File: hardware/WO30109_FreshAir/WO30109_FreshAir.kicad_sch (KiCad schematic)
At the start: 44 parts, among them K1 G5Q-1 DC12, K2 G5Q-1 DC12, K3 G5Q-1 DC12, K4 G5Q-1 DC12, P1 AC IN, P2 SWD, P3 AC OUT, Q1 Si2302CDS, Q2 Si2302CDS, Q3 Si2302CDS, Q4 Si2302CDS, U1 STM32F103C8T6, U2 IRM-02-12, U3 ZS3L, U4 LM1117-3.3

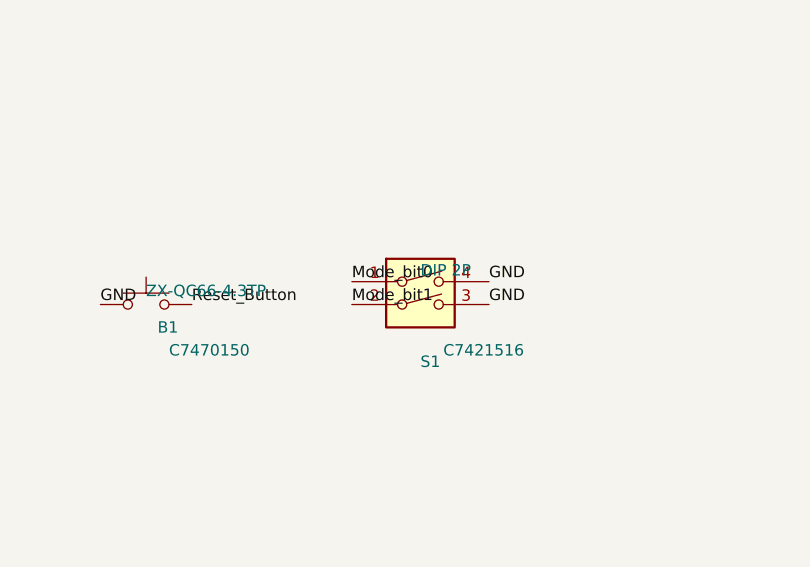
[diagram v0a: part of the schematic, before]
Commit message: feat: V1.3 PCB 由原 Gerber 轉入 KiCad＋安規 DRC 規則
- import_v13_pcb.py：走線/過孔照原樣、焊盤對齊放件、網路由銅箔連通推得
- 原理圖 vs 銅箔 0 衝突、parity 0；S1 Mode_bit 依銅箔修正
- .kicad_dru：市電↔SELV 6.4mm、市電間 2.5mm、板邊 0.5mm
- V1.3 DRC：253 個市電↔低壓違規（重現原設計問題）

Co-Authored-By: Claude Opus 5.5 (1M context) <noreply@anthropic.com>
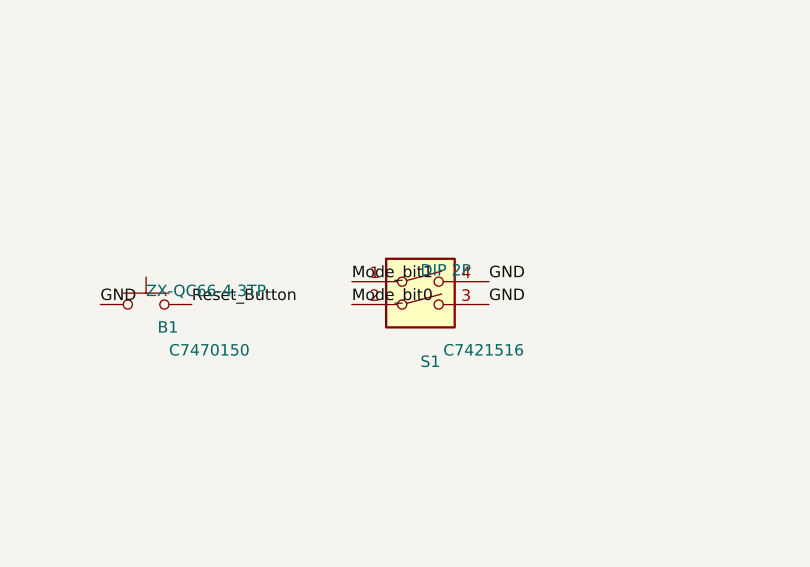
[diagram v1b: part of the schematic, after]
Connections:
- net Mode_bit0: now also S1.2; no longer S1.1
- net Mode_bit1: now also S1.1; no longer S1.2
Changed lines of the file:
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@@
 		(instances
 			(project "WO30109_FreshAir"
-				(path "/94552347-65ec-40ae-a746-f6e6e0667afa"
+				(path "/a2366431-4cde-4354-9495-6cae8083936f"
 					(reference "P1")
 					(unit 1)
@@
 		(instances
 			(project "WO30109_FreshAir"
-				(path "/94552347-65ec-40ae-a746-f6e6e0667afa"
+				(path "/a2366431-4cde-4354-9495-6cae8083936f"
 					(reference "U2")
 					(unit 1)
@@
 		(instances
 			(project "WO30109_FreshAir"
-				(path "/94552347-65ec-40ae-a746-f6e6e0667afa"
+				(path "/a2366431-4cde-4354-9495-6cae8083936f"
 					(reference "C6")
 					(unit 1)
@@
 		(instances
 			(project "WO30109_FreshAir"
-				(path "/94552347-65ec-40ae-a746-f6e6e0667afa"
+				(path "/a2366431-4cde-4354-9495-6cae8083936f"
 					(reference "U4")
 					(unit 1)
@@
 		(instances
 			(project "WO30109_FreshAir"
-				(path "/94552347-65ec-40ae-a746-f6e6e0667afa"
+				(path "/a2366431-4cde-4354-9495-6cae8083936f"
 					(reference "C7")
 					(unit 1)
@@
 		(instances
 			(project "WO30109_FreshAir"
-				(path "/94552347-65ec-40ae-a746-f6e6e0667afa"
+				(path "/a2366431-4cde-4354-9495-6cae8083936f"
 					(reference "U1")
 					(unit 1)
@@
 		(instances
 			(project "WO30109_FreshAir"
-				(path "/94552347-65ec-40ae-a746-f6e6e0667afa"
+				(path "/a2366431-4cde-4354-9495-6cae8083936f"
 					(reference "C1")
 					(unit 1)
@@
 		(instances
 			(project "WO30109_FreshAir"
-				(path "/94552347-65ec-40ae-a746-f6e6e0667afa"
+				(path "/a2366431-4cde-4354-9495-6cae8083936f"
 					(reference "C2")
 					(unit 1)
@@
 		(instances
 			(project "WO30109_FreshAir"
-				(path "/94552347-65ec-40ae-a746-f6e6e0667afa"
+				(path "/a2366431-4cde-4354-9495-6cae8083936f"
 					(reference "C3")
 					(unit 1)
@@
 		(instances
 			(project "WO30109_FreshAir"
-				(path "/94552347-65ec-40ae-a746-f6e6e0667afa"
+				(path "/a2366431-4cde-4354-9495-6cae8083936f"
 					(reference "C4")
 					(unit 1)
@@
 		(instances
 			(project "WO30109_FreshAir"
-				(path "/94552347-65ec-40ae-a746-f6e6e0667afa"
+				(path "/a2366431-4cde-4354-9495-6cae8083936f"
 					(reference "R1")
 					(unit 1)
@@
 		(instances
 			(project "WO30109_FreshAir"
-				(path "/94552347-65ec-40ae-a746-f6e6e0667afa"
+				(path "/a2366431-4cde-4354-9495-6cae8083936f"
 					(reference "C5")
 					(unit 1)
@@
 		(instances
 			(project "WO30109_FreshAir"
-				(path "/94552347-65ec-40ae-a746-f6e6e0667afa"
+				(path "/a2366431-4cde-4354-9495-6cae8083936f"
 					(reference "R2")
 					(unit 1)
@@
 		(instances
 			(project "WO30109_FreshAir"
-				(path "/94552347-65ec-40ae-a746-f6e6e0667afa"
+				(path "/a2366431-4cde-4354-9495-6cae8083936f"
 					(reference "R3")
 					(unit 1)
@@
 		(instances
 			(project "WO30109_FreshAir"
-				(path "/94552347-65ec-40ae-a746-f6e6e0667afa"
+				(path "/a2366431-4cde-4354-9495-6cae8083936f"
 					(reference "P2")
 					(unit 1)
@@
 		(instances
 			(project "WO30109_FreshAir"
-				(path "/94552347-65ec-40ae-a746-f6e6e0667afa"
+				(path "/a2366431-4cde-4354-9495-6cae8083936f"
 					(reference "U3")
 					(unit 1)
@@
 		(instances
 			(project "WO30109_FreshAir"
-				(path "/94552347-65ec-40ae-a746-f6e6e0667afa"
+				(path "/a2366431-4cde-4354-9495-6cae8083936f"
 					(reference "C8")
 					(unit 1)
@@
 		(instances
 			(project "WO30109_FreshAir"
-				(path "/94552347-65ec-40ae-a746-f6e6e0667afa"
+				(path "/a2366431-4cde-4354-9495-6cae8083936f"
 					(reference "C9")
 					(unit 1)
@@
 		(instances
 			(project "WO30109_FreshAir"
-				(path "/94552347-65ec-40ae-a746-f6e6e0667afa"
+				(path "/a2366431-4cde-4354-9495-6cae8083936f"
 					(reference "R4")
 					(unit 1)
@@
 		(instances
 			(project "WO30109_FreshAir"
-				(path "/94552347-65ec-40ae-a746-f6e6e0667afa"
+				(path "/a2366431-4cde-4354-9495-6cae8083936f"
 					(reference "L1")
 					(unit 1)
@@
 		(instances
 			(project "WO30109_FreshAir"
-				(path "/94552347-65ec-40ae-a746-f6e6e0667afa"
+				(path "/a2366431-4cde-4354-9495-6cae8083936f"
 					(reference "RF1")
 					(unit 1)
@@
 		(instances
 			(project "WO30109_FreshAir"
-				(path "/94552347-65ec-40ae-a746-f6e6e0667afa"
+				(path "/a2366431-4cde-4354-9495-6cae8083936f"
 					(reference "B1")
 					(unit 1)
@@
 		(instances
 			(project "WO30109_FreshAir"
-				(path "/94552347-65ec-40ae-a746-f6e6e0667afa"
+				(path "/a2366431-4cde-4354-9495-6cae8083936f"
 					(reference "S1")
 					(unit 1)
@@
 		(instances
 			(project "WO30109_FreshAir"
-				(path "/94552347-65ec-40ae-a746-f6e6e0667afa"
+				(path "/a2366431-4cde-4354-9495-6cae8083936f"
 					(reference "R5")
 					(unit 1)
@@
 		(instances
 			(project "WO30109_FreshAir"
-				(path "/94552347-65ec-40ae-a746-f6e6e0667afa"
+				(path "/a2366431-4cde-4354-9495-6cae8083936f"
 					(reference "R9")
 					(unit 1)
@@
 		(instances
 			(project "WO30109_FreshAir"
-				(path "/94552347-65ec-40ae-a746-f6e6e0667afa"
+				(path "/a2366431-4cde-4354-9495-6cae8083936f"
 					(reference "Q1")
 					(unit 1)
@@
 		(instances
 			(project "WO30109_FreshAir"
-				(path "/94552347-65ec-40ae-a746-f6e6e0667afa"
+				(path "/a2366431-4cde-4354-9495-6cae8083936f"
 					(reference "D1")
 					(unit 1)
@@
 		(instances
 			(project "WO30109_FreshAir"
-				(path "/94552347-65ec-40ae-a746-f6e6e0667afa"
+				(path "/a2366431-4cde-4354-9495-6cae8083936f"
 					(reference "K1")
 					(unit 1)
@@
 		(instances
 			(project "WO30109_FreshAir"
-				(path "/94552347-65ec-40ae-a746-f6e6e0667afa"
+				(path "/a2366431-4cde-4354-9495-6cae8083936f"
 					(reference "R6")
 					(unit 1)
@@
 		(instances
 			(project "WO30109_FreshAir"
-				(path "/94552347-65ec-40ae-a746-f6e6e0667afa"
+				(path "/a2366431-4cde-4354-9495-6cae8083936f"
 					(reference "R10")
 					(unit 1)
@@
 		(instances
 			(project "WO30109_FreshAir"
-				(path "/94552347-65ec-40ae-a746-f6e6e0667afa"
+				(path "/a2366431-4cde-4354-9495-6cae8083936f"
 					(reference "Q2")
 					(unit 1)
@@
 		(instances
 			(project "WO30109_FreshAir"
-				(path "/94552347-65ec-40ae-a746-f6e6e0667afa"
+				(path "/a2366431-4cde-4354-9495-6cae8083936f"
 					(reference "D2")
 					(unit 1)
@@
 		(instances
 			(project "WO30109_FreshAir"
-				(path "/94552347-65ec-40ae-a746-f6e6e0667afa"
+				(path "/a2366431-4cde-4354-9495-6cae8083936f"
 					(reference "K2")
 					(unit 1)
@@
 		(instances
 			(project "WO30109_FreshAir"
-				(path "/94552347-65ec-40ae-a746-f6e6e0667afa"
+				(path "/a2366431-4cde-4354-9495-6cae8083936f"
 					(reference "R7")
 					(unit 1)
@@
 		(instances
 			(project "WO30109_FreshAir"
-				(path "/94552347-65ec-40ae-a746-f6e6e0667afa"
+				(path "/a2366431-4cde-4354-9495-6cae8083936f"
 					(reference "R11")
 					(unit 1)
@@
 		(instances
 			(project "WO30109_FreshAir"
-				(path "/94552347-65ec-40ae-a746-f6e6e0667afa"
+				(path "/a2366431-4cde-4354-9495-6cae8083936f"
 					(reference "Q3")
 					(unit 1)
@@
 		(instances
 			(project "WO30109_FreshAir"
-				(path "/94552347-65ec-40ae-a746-f6e6e0667afa"
+				(path "/a2366431-4cde-4354-9495-6cae8083936f"
 					(reference "D3")
 					(unit 1)
@@
 		(instances
 			(project "WO30109_FreshAir"
-				(path "/94552347-65ec-40ae-a746-f6e6e0667afa"
+				(path "/a2366431-4cde-4354-9495-6cae8083936f"
 					(reference "K3")
 					(unit 1)
@@
 		(instances
 			(project "WO30109_FreshAir"
-				(path "/94552347-65ec-40ae-a746-f6e6e0667afa"
+				(path "/a2366431-4cde-4354-9495-6cae8083936f"
 					(reference "R8")
 					(unit 1)
@@
 		(instances
 			(project "WO30109_FreshAir"
-				(path "/94552347-65ec-40ae-a746-f6e6e0667afa"
+				(path "/a2366431-4cde-4354-9495-6cae8083936f"
 					(reference "R12")
 					(unit 1)
@@
 		(instances
 			(project "WO30109_FreshAir"
-				(path "/94552347-65ec-40ae-a746-f6e6e0667afa"
+				(path "/a2366431-4cde-4354-9495-6cae8083936f"
 					(reference "Q4")
 					(unit 1)
@@
 		(instances
 			(project "WO30109_FreshAir"
-				(path "/94552347-65ec-40ae-a746-f6e6e0667afa"
+				(path "/a2366431-4cde-4354-9495-6cae8083936f"
 					(reference "D4")
 					(unit 1)
@@
 		(instances
 			(project "WO30109_FreshAir"
-				(path "/94552347-65ec-40ae-a746-f6e6e0667afa"
+				(path "/a2366431-4cde-4354-9495-6cae8083936f"
 					(reference "K4")
 					(unit 1)
@@
 		(instances
 			(project "WO30109_FreshAir"
-				(path "/94552347-65ec-40ae-a746-f6e6e0667afa"
+				(path "/a2366431-4cde-4354-9495-6cae8083936f"
 					(reference "P3")
 					(unit 1)
@@
 		(instances
 			(project "WO30109_FreshAir"
-				(path "/94552347-65ec-40ae-a746-f6e6e0667afa"
+				(path "/a2366431-4cde-4354-9495-6cae8083936f"
 					(reference "#FLG01")
 					(unit 1)
@@
 		(instances
 			(project "WO30109_FreshAir"
-				(path "/94552347-65ec-40ae-a746-f6e6e0667afa"
+				(path "/a2366431-4cde-4354-9495-6cae8083936f"
 					(reference "#FLG02")
 					(unit 1)
@@
 		)
 	)
-	(label "Mode_bit0"
+	(label "Mode_bit1"
 		(at 322.58 101.6 0)
 		(effects
@@
 		)
 	)
-	(label "Mode_bit1"
+	(label "Mode_bit0"
 		(at 322.58 104.14 0)
 		(effects

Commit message: feat(v2.0): 原理圖改版 — 保險絲/壓敏電阻、降壓電源、ZS3L UART
- F1 T3.15A 慢斷保險絲（AC_L 入口）、RV1 07D471K 壓敏電阻
- U4 LM1117 -> AP63203WU 3.3V 降壓（L2 3.9uH、C7/C13 22uF、C12 BST 100nF，依規格書 Table 2）
- 12V 預算 146mA < IRM-02-12 167mA，保留原電源
- ZS3L TXD->PA10、RXD<-PA9（USART1）、RST<-PB1(+R13 10k)；LED 改 PB0
- NRST 電容 1uF->100nF、VDDA 加 C10 1uF、BOOT0 測試點 TP1
- ERC 0 error

Co-Authored-By: Claude Opus 5.5 (1M context) <noreply@anthropic.com>
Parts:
- removed U4: LM1117-3.3, Package_TO_SOT_SMD:SOT-223-3_TabPin2, symbol Regulator_Linear:AMS1117-3.3
- added C10: 1uF, Capacitor_SMD:C_0603_1608Metric, symbol Device:C
- added C12, C14: 100nF, Capacitor_SMD:C_0603_1608Metric, symbol Device:C
- added C13: 22uF 25V, Capacitor_SMD:C_0805_2012Metric, symbol Device:C
- added F1: T3.15A 250V, Fuse:Fuseholder_TR5_Littelfuse_No560_No460, symbol Device:Fuse
- added L2: 3.9uH, Inductor_SMD:L_Sunlord_SWPA4030S, symbol Device:L
- added R13: 10k, Resistor_SMD:R_0603_1608Metric, symbol Device:R
- added RV1: 07D471K, Varistor:RV_Disc_D7mm_W3.4mm_P5mm, symbol Device:Varistor
- added TP1: BOOT0, TestPoint:TestPoint_Pad_D1.5mm, symbol Connector:TestPoint
- added U4: AP63203WU-7, Package_TO_SOT_SMD:TSOT-23-6, symbol Regulator_Switching:AP63203WU
- C5: value 1uF -> 100nF; LCSC C15849 -> C14663
- C7: value 10uF -> 22uF 25V; footprint Capacitor_SMD:C_0603_1608Metric -> Capacitor_SMD:C_0805_2012Metric; LCSC C96446 -> C45783
- P1: value AC IN -> AC IN 230V
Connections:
- net +12V: now also C14.1, U4.2 (EN), U4.3 (IN)
- net +3V3: now also C10.1, C13.1, L2.2, R13.1, U4.1 (FB)
- net AC_L: now also F1.2, RV1.1; no longer P1.1 (Pin_1)
- net AC_N: now also RV1.2
- net BOOT0: now also TP1.1
- net GND: now also C10.2, C13.2, C14.2, U4.4 (GND)
- net LED: now reaches U1.18 (PB0)
- net LED: now also R4.1
- net ZB_RST: now reaches U1.19 (PB1)
- net ZB_RST: now also U3.1 (RST), R13.2
- net ZB_RX: now reaches U1.30 (PA9)
- net ZB_RX: now also U3.15 (RXD)
- net ZB_TX: now reaches U1.31 (PA10)
- net ZB_TX: now also U3.16 (TXD)
- removed net NET_LED: R4.1, U3.16 (TXD)
- new net AC_L_IN: F1.1, P1.1 (Pin_1)
- new net BST: C12.1, U4.6 (BST)
- new net SW: C12.2, L2.1, U4.5 (SW)
- no-connect marks 22 -> 16

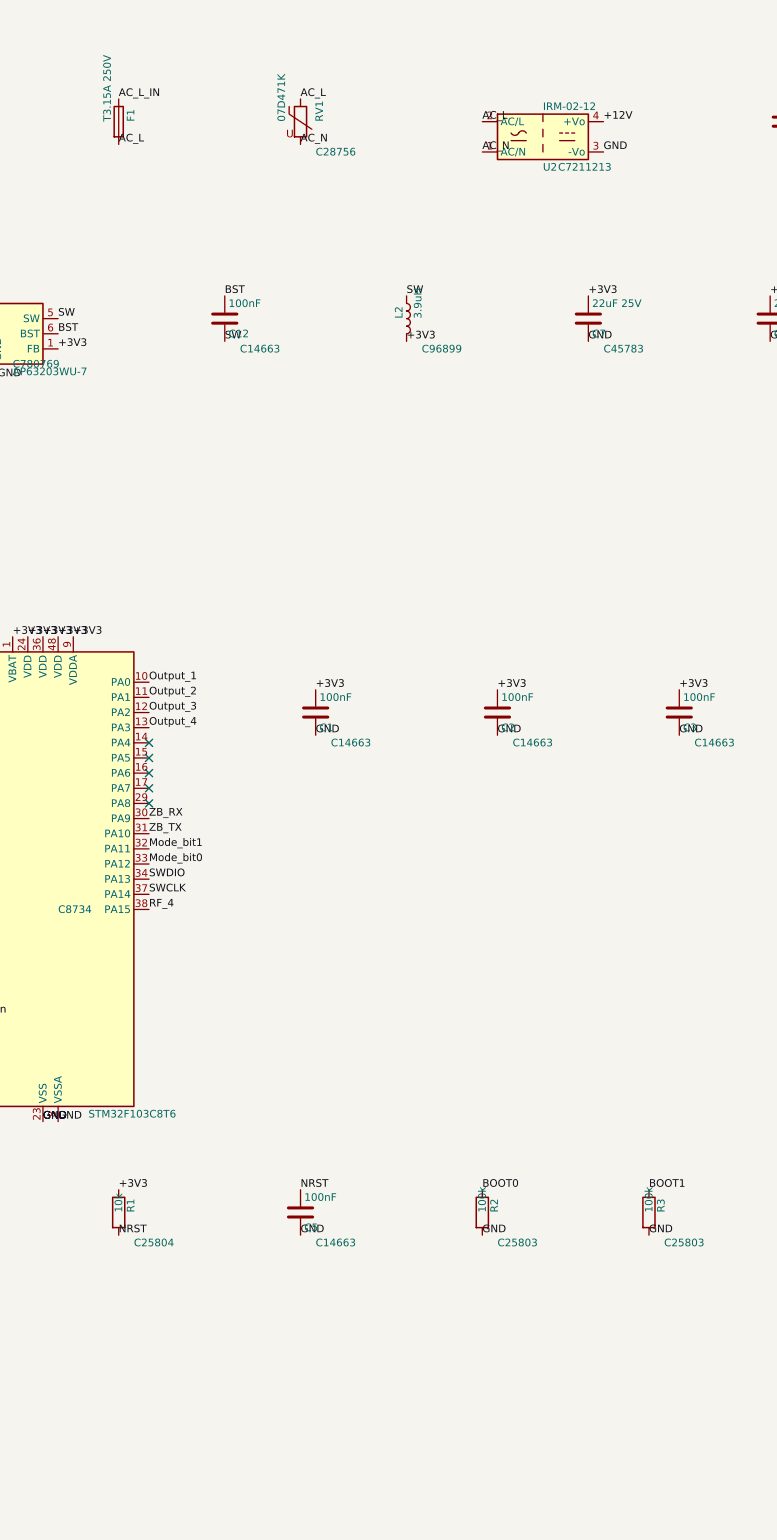
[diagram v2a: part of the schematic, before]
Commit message: feat(v2.0): PCB 安規改版完成 — DRC 0 錯誤、全部接通
PCB
- 市電↔低壓 ≥6.4mm、市電網路間 ≥1.5mm、板邊 ≥0.5mm（.kicad_dru 規則）
- 新增固定孔到市電 ≥2.3mm 規則；右緣市電走道外移、AC_N 在 H2 旁內彎（H2 0.85→2.85mm）
- F1/RV1、AP63203 降壓、繼電器驅動、RF1/P2/S1 重新擺放；H1–H4 固定孔
- 繼電器輸出 DO_* 由 mains_router 雙層格點佈線；低壓由 Freerouting，剩餘由 route_leftovers 補
- GND 鋪銅依規則自動退讓；LCSC 料號不印絲印

工具與文件
- scripts/build_v20.sh 一鍵重建（多組 Freerouting 設定，取第一組全接通）
- .github/workflows/kicad-ci.yml：ERC/DRC/生產檔
- README：架構、改版、安規、版控、CI、範例（mermaid 圖）＋板子圖片
- docs/review：V1.3 設計審查

驗證（kicad-cli 10.0.6）：ERC 0、DRC 0 錯誤、0 未連線、0 parity

Co-Authored-By: Claude Opus 5.5 (1M context) <noreply@anthropic.com>
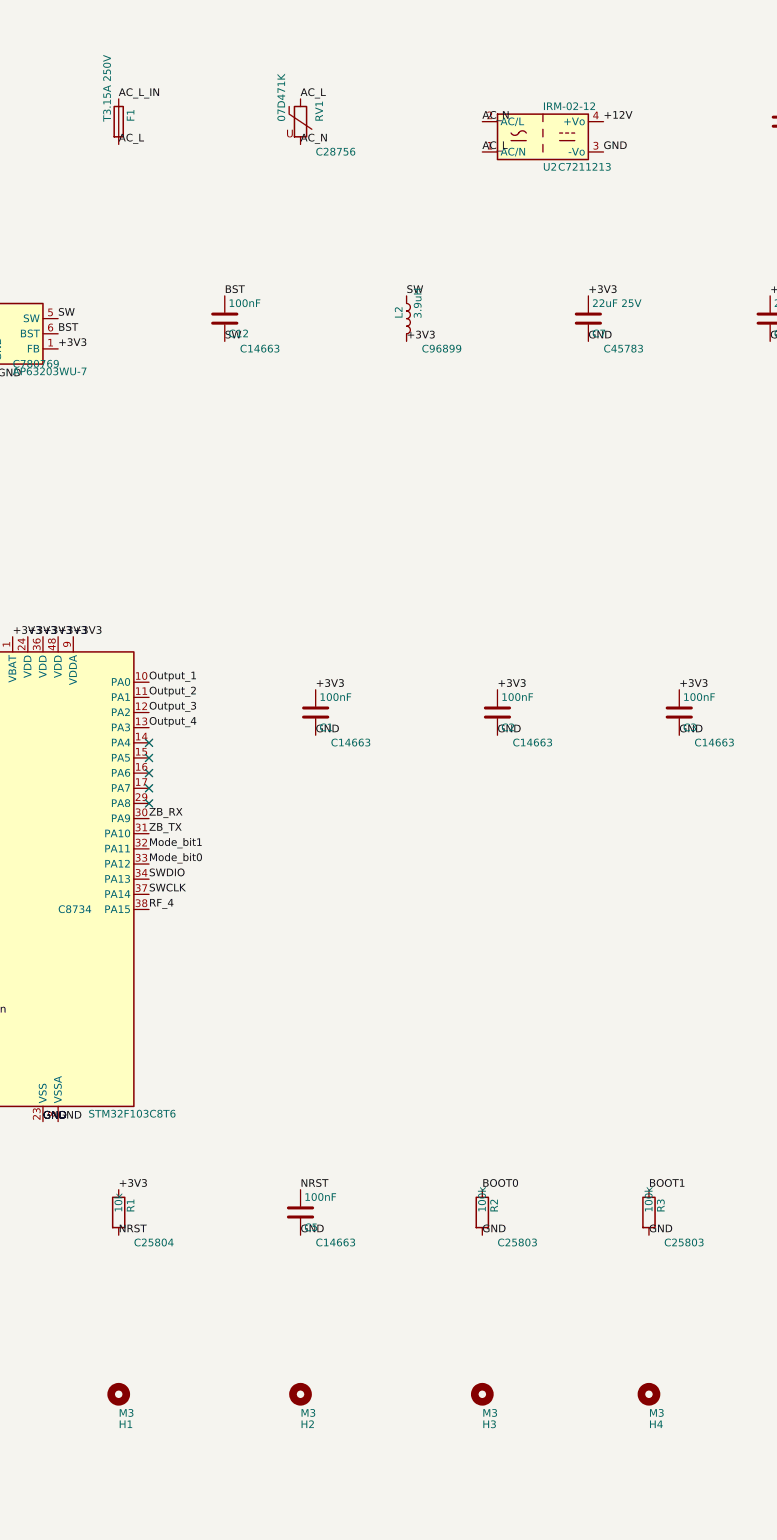
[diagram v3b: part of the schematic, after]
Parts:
- added H1, H2, H3, H4: M3, MountingHole:MountingHole_3.2mm_M3, symbol Mechanical:MountingHole
- K1, K2, K3, K4: footprint Relay_THT:Relay_SPDT_Omron-G5Q-1 -> WOOW:Relay_SPDT_Omron-G5Q-1_Tight
- TP1: now left out of the parts list
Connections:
- net AC_L: now also U2.1 (AC/N); no longer U2.2 (AC/L)
- net AC_N: now also U2.2 (AC/L); no longer U2.1 (AC/N)

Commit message: feat(v3.0): Tuya ZS3L＋EPA09-4D → ESP32-C6 單晶片＋SYN480R
- U1 STM32F103＋U3 ZS3L → ESP32-C6-WROOM-1-N8（C5366877，Zigbee 3.0，JLC 有庫存）
- RF1 EPA09-4D → SYN480R（C916347）＋13.52127MHz 晶振＋LC 匹配，韌體解 EV1527
- B1 改 IO9（BOOT），P2 改 2×3 燒錄座；ANT1 433MHz 天線焊點
- PCB 從 v2.0 標籤開始，只動低壓區；build_v30.sh 一鍵重建
- 檢查：ERC 0 錯誤、DRC 0 錯誤、0 未連線、parity 0

Co-Authored-By: Claude Opus 5.5 (1M context) <noreply@anthropic.com>
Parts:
- removed C10: 1uF, Capacitor_SMD:C_0603_1608Metric, symbol Device:C
- removed C3, C4: 100nF, Capacitor_SMD:C_0603_1608Metric, symbol Device:C
- removed P2: SWD, Connector_PinHeader_2.54mm:PinHeader_1x04_P2.54mm_Vertical, symbol Connector_Generic:Conn_01x04
- removed R13: 10k, Resistor_SMD:R_0603_1608Metric, symbol Device:R
- removed RF1: EPA09-4D, WOOW:Ebelong_EPA09-4D, symbol WOOW:EPA09-4D
- removed TP1: BOOT0, TestPoint:TestPoint_Pad_D1.5mm, symbol Connector:TestPoint
- removed U1: STM32F103C8T6, Package_QFP:LQFP-48_7x7mm_P0.5mm, symbol MCU_ST_STM32F1:STM32F103C8Tx
- removed U3: ZS3L, WOOW:Tuya_ZS3L, symbol WOOW:ZS3L
- added ANT1: 433MHz 1/4λ 17.3cm, TestPoint:TestPoint_THTPad_D2.0mm_Drill1.0mm, symbol Connector:Conn_01x01_Pin
- added C15: 6.8pF C0G, Capacitor_SMD:C_0603_1608Metric, symbol Device:C
- added C16: 1.8pF C0G, Capacitor_SMD:C_0603_1608Metric, symbol Device:C
- added C17: 1uF, Capacitor_SMD:C_0603_1608Metric, symbol Device:C
- added L3: 27nH, Inductor_SMD:L_0603_1608Metric, symbol Device:L
- added L4: 47nH, Inductor_SMD:L_0603_1608Metric, symbol Device:L
- added P2: PROG, Connector_PinHeader_2.54mm:PinHeader_2x03_P2.54mm_Vertical, symbol Connector_Generic:Conn_02x03_Odd_Even
- added R14: 0R, Resistor_SMD:R_0603_1608Metric, symbol Device:R
- added U1: ESP32-C6-WROOM-1-N8, WOOW:Espressif_ESP32-C6-WROOM-1, symbol WOOW:ESP32-C6-WROOM-1
- added U3: SYN480R, Package_SO:SOIC-8_3.9x4.9mm_P1.27mm, symbol WOOW:SYN480R
- added Y1: 13.52127MHz 20pF, Crystal:Crystal_SMD_3225-4Pin_3.2x2.5mm, symbol WOOW:Crystal_4P
- C1: value 100nF -> 22uF 25V; footprint Capacitor_SMD:C_0603_1608Metric -> Capacitor_SMD:C_0805_2012Metric; LCSC C14663 -> C45783
- C5: value 100nF -> 1uF; LCSC C14663 -> C15849
- R2, R3: value 100k -> 10k; LCSC C25803 -> C25804
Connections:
- net BOOT0 is gone; now on net +3V3: R2.1
- net BOOT1 is gone; now on net +3V3: R3.1
- net +3V3: now also C17.1, P2.1 (Pin_1), U1.2 (3V3), U3.3 (VDD)
- net GND: now also C16.2, C17.2, L3.2, L4.2, P2.2 (Pin_2), R14.2, U1.1 (GND), U1.28 (GND), U1.29 (GND), U3.1 (GND), U3.6 (SHUT), Y1.2 (GND), Y1.3 (X2), Y1.4 (GND); no longer R2.2, R3.2
- net LED: now also U1.27 (IO2)
- net Mode_bit0: now also U1.11 (IO10)
- net Mode_bit1: now also U1.12 (IO11)
- net Relay_1: now also U1.6 (IO6)
- net Relay_2: now also U1.7 (IO7)
- net Relay_3: now also U1.8 (IO0)
- net Relay_4: now also U1.9 (IO1)
- net NRST renamed EN
- net EN: now also P2.5 (Pin_5), U1.3 (EN)
- net Reset_Button renamed BOOT
- net BOOT: now also R2.2, P2.6 (Pin_6), U1.15 (IO9)
- new net IO8: R3.2, U1.10 (IO8)
- new net RF_ANT: ANT1.1 (Pin_1), C15.1, C16.1, L3.1
- new net RF_DATA: U1.21 (IO23), U3.5 (DO)
- new net RF_IN: C15.2, L4.1, U3.2 (ANT)
- new net RF_SQ: R14.1, U3.7 (SQ)
- new net RF_XTAL: U3.8 (RO), Y1.1 (X1)
- new net U0RXD: P2.4 (Pin_4), U1.24 (RXD0/IO17)
- new net U0TXD: P2.3 (Pin_3), U1.25 (TXD0/IO16)
- no-connect marks 16 -> 15
